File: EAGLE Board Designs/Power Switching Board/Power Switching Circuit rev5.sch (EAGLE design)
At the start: 63 parts, among them J1 CONNECTOR-4_SOURIAU_, J2 CONNECTOR-3_8STA20435PN, J3 CONNECTOR-4_SOURIAU_, K1 RELAY_SOLIDSTATE_NO_CMX60D20, Q1 TRANSISTOR_N_MOS_2-7K1S_TK100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, Q2 TRANSISTOR_N_MOS_2-7K1S_TK100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, Q3 TRANSISTOR_N_MOS_2-7K1S_TK100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, Q4 TRANSISTOR_N_MOS_2-7K1S_TK100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, U1 LTC4421

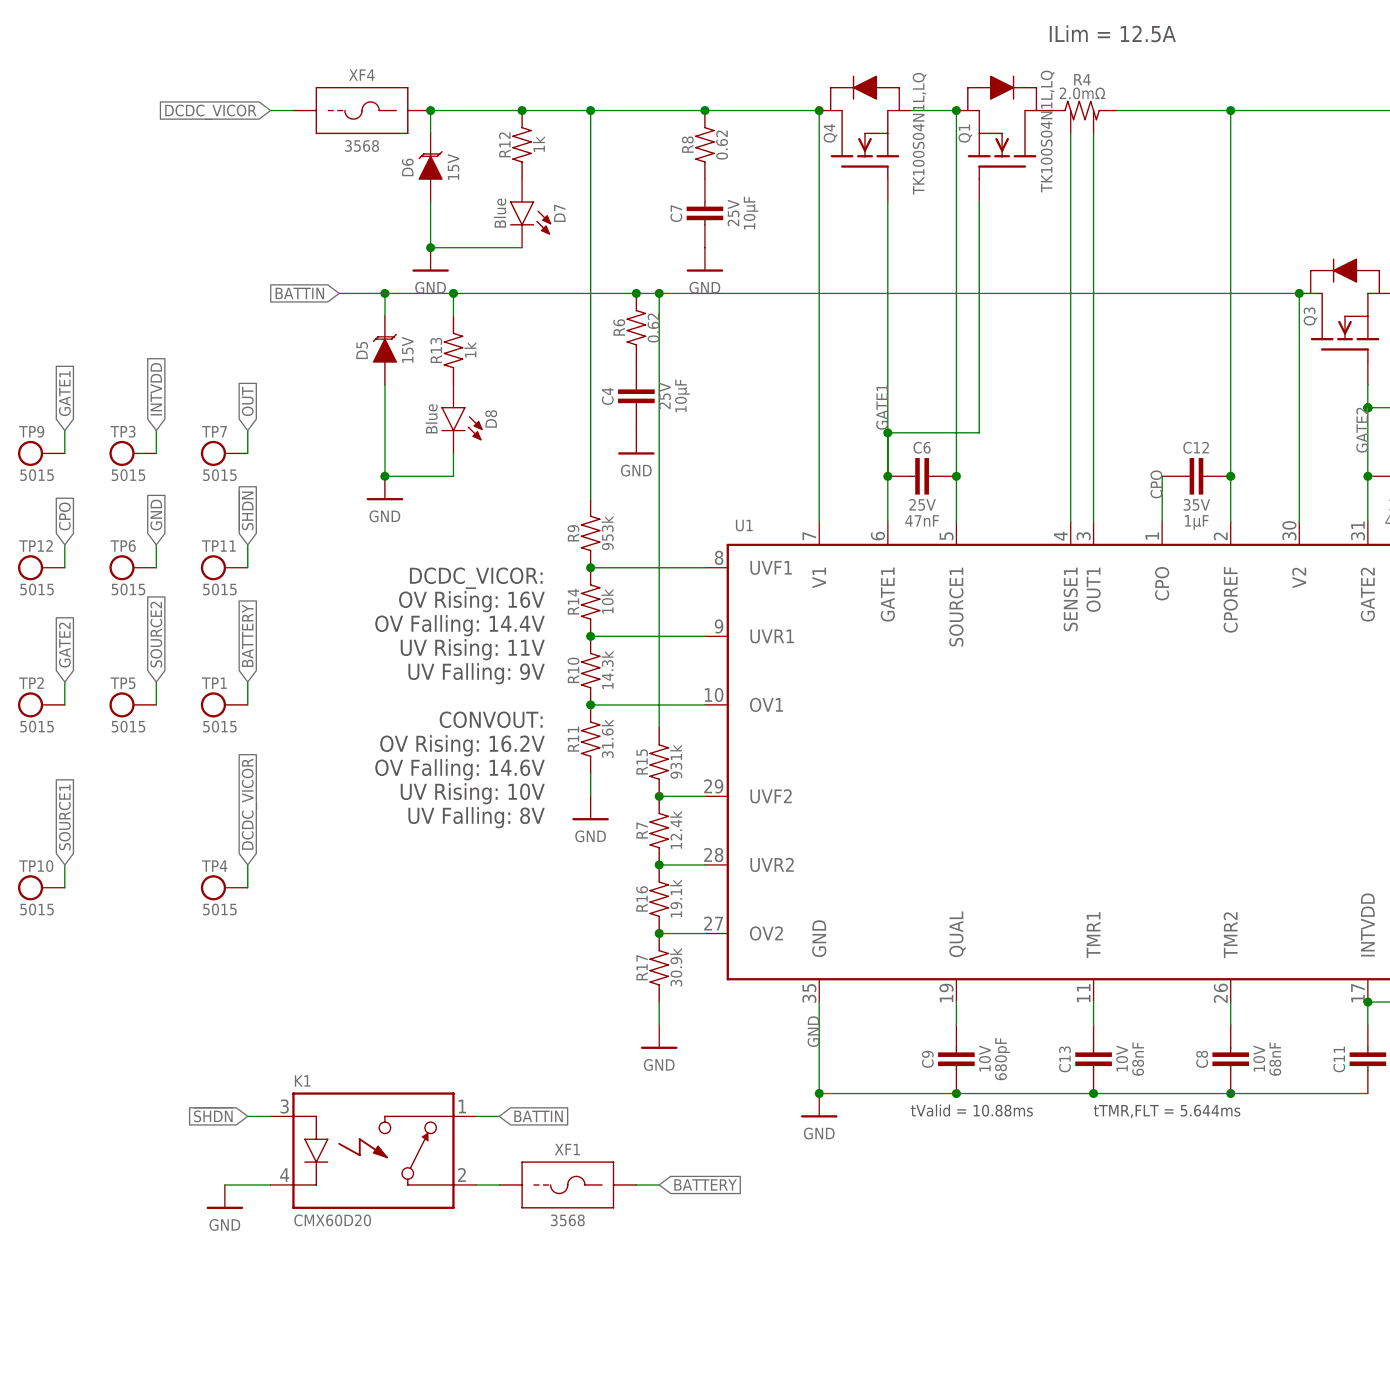
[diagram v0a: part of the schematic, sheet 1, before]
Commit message: Fixed issues with order of inputs to SSR
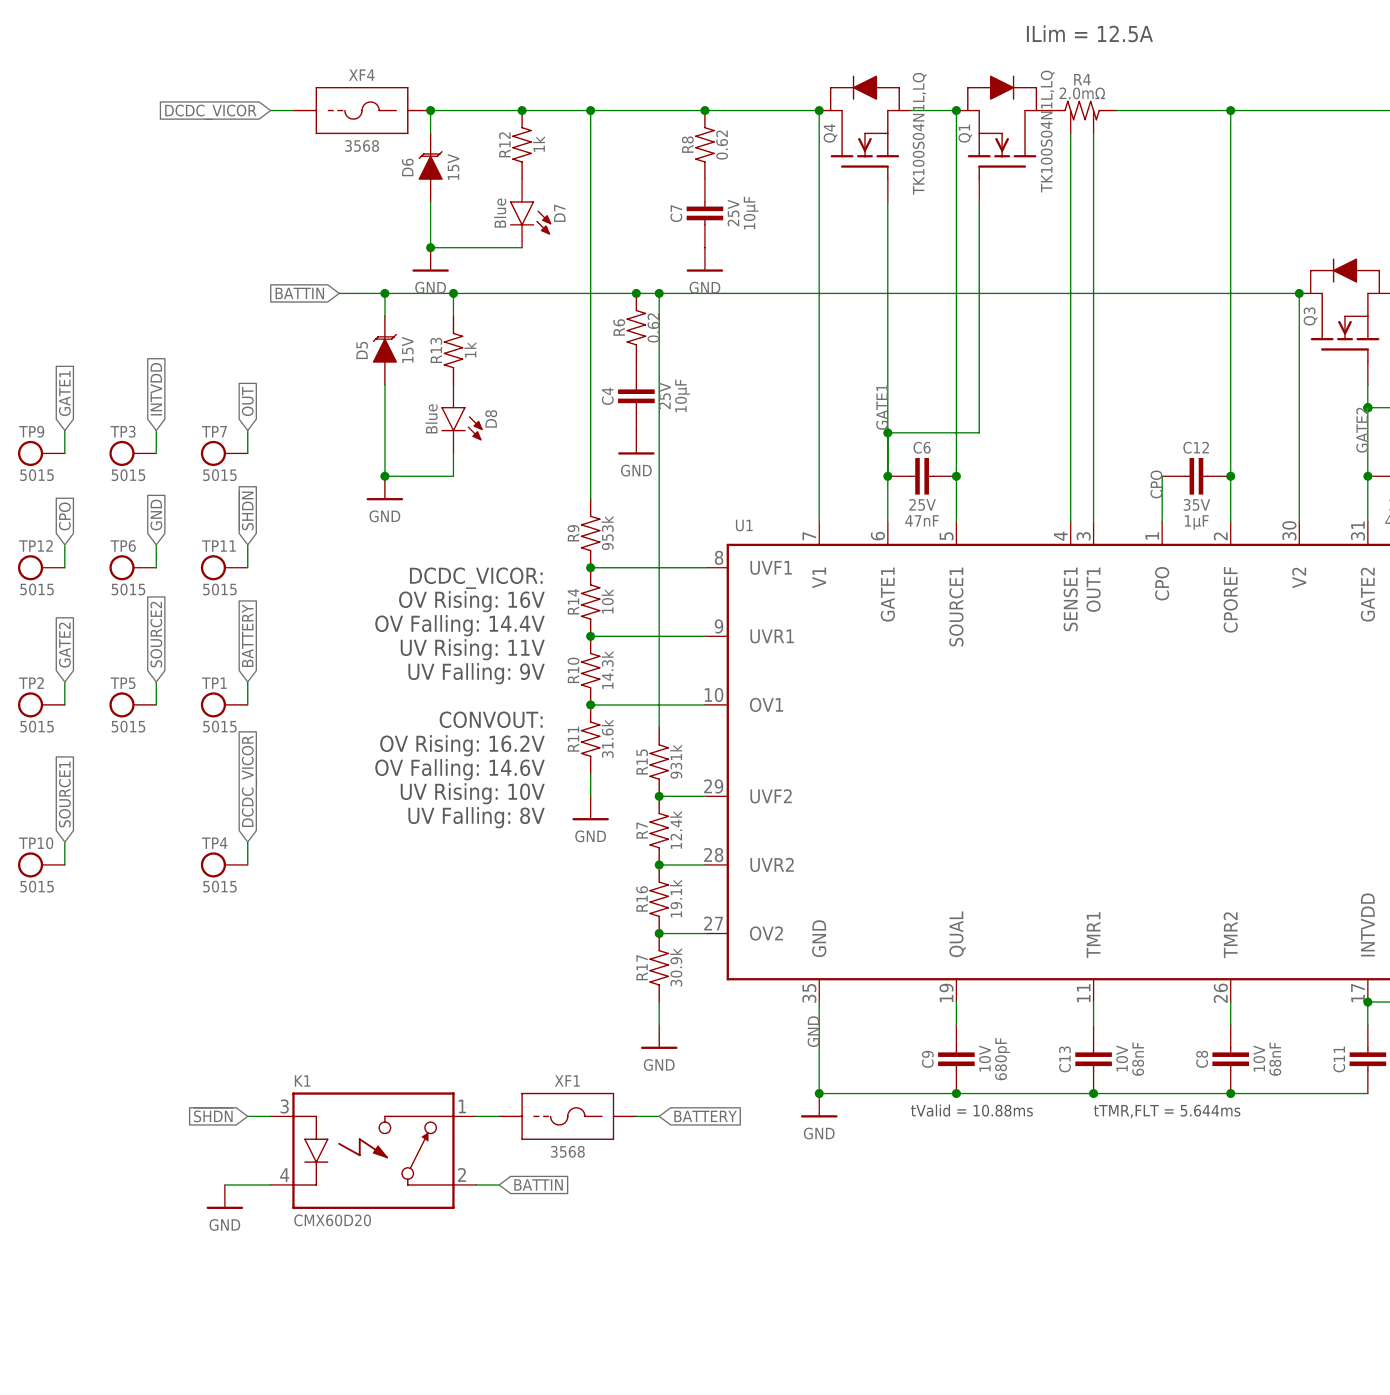
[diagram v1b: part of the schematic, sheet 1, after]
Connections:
- removed net N$12: K1.CONTACT1, XF1.1
- new net N$8: K1.CONTACT2, XF1.1
- net BATTIN: now also K1.CONTACT1; no longer K1.CONTACT2
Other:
- moved on the sheet: TP10, TP4, XF1
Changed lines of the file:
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@@
 <part name="P15" library="HyTechSupplies" deviceset="GND" device=""/>
 <part name="FRAME1" library="HyTechFrames" deviceset="FRAME" device="">
-<attribute name="DESCRIPTION_1" value="Circuit is used to switch the active power source of  the vehicle from the GLV battery to the accumulator"/>
+<attribute name="DESCRIPTION_1" value="Circuit is used to switch the active power source"/>
+<attribute name="DESCRIPTION_2" value="of  the vehicle from the GLV battery to the accumulator"/>
 <attribute name="DESIGNER_BOARD" value="Steven Elias"/>
 <attribute name="DESIGNER_SCHEMATIC" value="Steven Elias"/>
@@
 <part name="R1" library="HyTechDevices" deviceset="RESISTOR_?_*" device="0603" technology="10K"/>
 <part name="XF2" library="HyTechDevices" deviceset="FUSE_HOLDER_*" device="PTH" technology="MINIBLADE"/>
-<part name="XF1" library="HyTechDevices" deviceset="FUSE_HOLDER_*" device="PTH" technology="MINIBLADE"/>
 <part name="XF3" library="HyTechDevices" deviceset="FUSE_HOLDER_*" device="PTH" technology="MINIBLADE"/>
 <part name="XF4" library="HyTechDevices" deviceset="FUSE_HOLDER_*" device="PTH" technology="MINIBLADE"/>
@@
 <part name="R16" library="HyTechDevices" deviceset="RESISTOR_?_*" device="0805" technology="19.1K"/>
 <part name="R17" library="HyTechDevices" deviceset="RESISTOR_?_*" device="0603" technology="30.9K"/>
+<part name="XF1" library="HyTechDevices" deviceset="FUSE_HOLDER_*" device="PTH" technology="MINIBLADE"/>
 </parts>
 <sheets>
@@
 <text x="-35.56" y="-73.66" size="1.27" layer="97">tValid = 10.88ms</text>
 <text x="-15.24" y="-73.66" size="1.27" layer="97">tTMR,FLT = 5.644ms</text>
-<text x="-20.32" y="45.72" size="1.778" layer="97">ILim = 12.5A</text>
+<text x="-22.86" y="45.72" size="1.778" layer="97">ILim = 12.5A</text>
 <text x="33.02" y="25.4" size="1.778" layer="97">ILim = 12.5A</text>
 <text x="68.58" y="-10.16" size="1.778" layer="97">VALID1: DCDC_VICOR is within OV/UV for time tValid
@@
 <attribute name="REVIEWER_BOARD" x="80.01" y="-119.38" size="2.54" layer="95"/>
 <attribute name="REVIEWER_FURTHER" x="80.01" y="-127" size="2.54" layer="95"/>
-<attribute name="DESCRIPTION_1" x="46.99" y="-147.32" size="2.54" layer="95"/>
+<attribute name="DESCRIPTION_1" x="49.53" y="-142.24" size="2.54" layer="95"/>
 <attribute name="DESCRIPTION_2" x="29.21" y="-147.32" size="2.54" layer="95"/>
 </instance>
@@
 <attribute name="MPN" x="-116.078" y="-129.54" size="1.27" layer="96" rot="R90" align="top-center"/>
 </instance>
-<instance part="XF1" gate="G$1" x="-73.66" y="-78.74" smashed="yes">
-<attribute name="NAME" x="-73.66" y="-77.978" size="1.27" layer="95" align="bottom-center"/>
-<attribute name="MPN" x="-73.66" y="-84.582" size="1.27" layer="96" align="top-center"/>
-</instance>
 <instance part="XF3" gate="G$1" x="109.22" y="40.64" smashed="yes">
 <attribute name="NAME" x="109.22" y="41.402" size="1.27" layer="95" align="bottom-center"/>
@@
 <attribute name="MPN" x="-114.3" y="-1.778" size="1.27" layer="95" align="top-left"/>
 </instance>
-<instance part="TP4" gate="G$1" x="-111.76" y="-48.26" smashed="yes">
-<attribute name="NAME" x="-114.3" y="-46.482" size="1.27" layer="95"/>
-<attribute name="MPN" x="-114.3" y="-50.038" size="1.27" layer="95" align="top-left"/>
-</instance>
-<instance part="TP10" gate="G$1" x="-132.08" y="-48.26" smashed="yes">
-<attribute name="NAME" x="-134.62" y="-46.482" size="1.27" layer="95"/>
-<attribute name="MPN" x="-134.62" y="-50.038" size="1.27" layer="95" align="top-left"/>
+<instance part="TP4" gate="G$1" x="-111.76" y="-45.72" smashed="yes">
+<attribute name="NAME" x="-114.3" y="-43.942" size="1.27" layer="95"/>
+<attribute name="MPN" x="-114.3" y="-47.498" size="1.27" layer="95" align="top-left"/>
+</instance>
+<instance part="TP10" gate="G$1" x="-132.08" y="-45.72" smashed="yes">
+<attribute name="NAME" x="-134.62" y="-43.942" size="1.27" layer="95"/>
+<attribute name="MPN" x="-134.62" y="-47.498" size="1.27" layer="95" align="top-left"/>
 </instance>
 <instance part="D4" gate="G$1" x="93.98" y="33.02" smashed="yes" rot="R90">
@@
 <attribute name="NAME" x="-64.77" y="-57.15" size="1.27" layer="95" rot="R90" align="bottom-center"/>
 <attribute name="RESISTANCE" x="-62.23" y="-57.15" size="1.27" layer="96" rot="R90" align="top-center"/>
+</instance>
+<instance part="XF1" gate="G$1" x="-73.66" y="-71.12" smashed="yes">
+<attribute name="NAME" x="-73.66" y="-70.358" size="1.27" layer="95" align="bottom-center"/>
+<attribute name="MPN" x="-73.66" y="-76.962" size="1.27" layer="96" align="top-center"/>
 </instance>
 </instances>
@@
 </segment>
 </net>
-<net name="N$12" class="0">
-<segment>
-<wire x1="-81.28" y1="-81.28" x2="-83.82" y2="-81.28" width="0.1524" layer="91"/>
-<pinref part="XF1" gate="G$1" pin="1"/>
-<pinref part="K1" gate="G$1" pin="CONTACT1"/>
-</segment>
-</net>
 <net name="N$22" class="0">
 <segment>
@@
 </segment>
 <segment>
-<wire x1="-66.04" y1="-81.28" x2="-63.5" y2="-81.28" width="0.1524" layer="91"/>
-<label x="-63.5" y="-81.28" size="1.27" layer="95" xref="yes"/>
-<pinref part="XF1" gate="G$1" pin="2"/>
-</segment>
-<segment>
 <pinref part="TP1" gate="G$1" pin="1"/>
 <wire x1="-109.22" y1="-27.94" x2="-109.22" y2="-25.4" width="0.1524" layer="91"/>
 <label x="-109.22" y="-25.4" size="1.27" layer="95" rot="R90" xref="yes"/>
+</segment>
+<segment>
+<wire x1="-66.04" y1="-73.66" x2="-63.5" y2="-73.66" width="0.1524" layer="91"/>
+<label x="-63.5" y="-73.66" size="1.27" layer="95" xref="yes"/>
+<pinref part="XF1" gate="G$1" pin="2"/>
 </segment>
 </net>
@@
 <segment>
 <pinref part="TP4" gate="G$1" pin="1"/>
-<wire x1="-109.22" y1="-48.26" x2="-109.22" y2="-45.72" width="0.1524" layer="91"/>
-<label x="-109.22" y="-45.72" size="1.27" layer="95" rot="R90" xref="yes"/>
+<wire x1="-109.22" y1="-45.72" x2="-109.22" y2="-43.18" width="0.1524" layer="91"/>
+<label x="-109.22" y="-43.18" size="1.27" layer="95" rot="R90" xref="yes"/>
 </segment>
 </net>
@@
 <segment>
 <pinref part="TP10" gate="G$1" pin="1"/>
-<wire x1="-129.54" y1="-48.26" x2="-129.54" y2="-45.72" width="0.1524" layer="91"/>
-<label x="-129.54" y="-45.72" size="1.27" layer="95" rot="R90" xref="yes"/>
+<wire x1="-129.54" y1="-45.72" x2="-129.54" y2="-43.18" width="0.1524" layer="91"/>
+<label x="-129.54" y="-43.18" size="1.27" layer="95" rot="R90" xref="yes"/>
 </segment>
 <segment>
@@
 </segment>
 <segment>
-<wire x1="-83.82" y1="-73.66" x2="-81.28" y2="-73.66" width="0.1524" layer="91"/>
-<label x="-81.28" y="-73.66" size="1.27" layer="95" xref="yes"/>
+<wire x1="-83.82" y1="-81.28" x2="-81.28" y2="-81.28" width="0.1524" layer="91"/>
+<label x="-81.28" y="-81.28" size="1.27" layer="95" xref="yes"/>
+<pinref part="K1" gate="G$1" pin="CONTACT1"/>
+</segment>
+</net>
+<net name="N$8" class="0">
+<segment>
+<wire x1="-81.28" y1="-73.66" x2="-83.82" y2="-73.66" width="0.1524" layer="91"/>
+<pinref part="XF1" gate="G$1" pin="1"/>
 <pinref part="K1" gate="G$1" pin="CONTACT2"/>
 </segment>
